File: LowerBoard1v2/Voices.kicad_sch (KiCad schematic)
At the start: 52 parts, among them J701 VoiceBoardConn_20P_200P, J702 VoiceBoardConn_20P_200P, J703 VoiceBoardConn_20P_200P, J704 VoiceBoardConn_20P_200P, J705 VoiceBoardConn_20P_200P, J706 VoiceBoardConn_20P_200P, J707 VoiceBoardConn_20P_200P, J708 VoiceBoardConn_20P_200P, U701 TCA9548APWR, U703 L7805, U704 L7905

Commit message: switched to resistor arrays for schematic
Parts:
- removed J702, J703, J704, J705, J706, J707, J708: VoiceBoardConn_20P_200P, Connector_PinHeader_2.00mm:PinHeader_2x10_P2.00mm_Vertical, symbol Connector_Audio:VoiceBoardConn_20P_200P
- removed R704, R705, R706, R707, R708, R709, R710, R711, R712, R713, R714, R715, R717, R718, R719, R720: 2k2, Resistor_SMD:R_0805_2012Metric, symbol Device:R_US
- added J502, J503, J504, J505, J506, J507, J508: VoiceBoardConn_20P_200P, Connector_PinHeader_2.00mm:PinHeader_2x10_P2.00mm_Vertical, symbol Connector_Audio:VoiceBoardConn_20P_200P
- added RN501, RN502, RN503, RN504: 2k2, Resistor_SMD:R_Array_Concave_4x0603, symbol Device:R_Pack04_Split
- renumbered C702 to C501, C705 to C502, C703 to C503, C704 to C504, C701 to C505, J701 to J501, R701 to R501, R702 to R502, R703 to R503, R716 to R504, TP701 to TP501, TP702 to TP502, TP703 to TP503, TP704 to TP504, TP705 to TP505, TP706 to TP506, TP715 to TP507, TP716 to TP508, TP707 to TP509, TP708 to TP510, TP709 to TP511, TP710 to TP512, TP711 to TP513, TP712 to TP514, TP713 to TP515, TP714 to TP516, U703 to U501, U704 to U502, U701 to U503
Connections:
- net +12V: now also J502.17 (+12V), J503.17 (+12V), J504.17 (+12V), J505.17 (+12V), J506.17 (+12V), J507.17 (+12V), J508.17 (+12V)
- net +3.3V: now also J502.15 (+3V3), J503.15 (+3V3), J504.15 (+3V3), J505.15 (+3V3), J506.15 (+3V3), J507.15 (+3V3), J508.15 (+3V3), RN501.5 (R4.2), RN501.6 (R3.2), RN501.7 (R2.2), RN501.8 (R1.2), RN502.5 (R4.2), RN502.6 (R3.2), RN502.7 (R2.2), RN502.8 (R1.2), RN503.5 (R4.2), RN503.6 (R3.2), RN503.7 (R2.2), RN503.8 (R1.2), RN504.5 (R4.2), RN504.6 (R3.2), RN504.7 (R2.2), RN504.8 (R1.2)
- net +5V: now also J502.19 (+5V), J503.19 (+5V), J504.19 (+5V), J505.19 (+5V), J506.19 (+5V), J507.19 (+5V), J508.19 (+5V)
- net -12V: now also J502.18 (-12V), J503.18 (-12V), J504.18 (-12V), J505.18 (-12V), J506.18 (-12V), J507.18 (-12V), J508.18 (-12V)
- net -5V: now also J502.20 (-5V), J503.20 (-5V), J504.20 (-5V), J505.20 (-5V), J506.20 (-5V), J507.20 (-5V), J508.20 (-5V)
- net CUTOFF_V2: now also J502.12 (VCF)
- net CUTOFF_V3: now also J503.12 (VCF)
- net CUTOFF_V4: now also J504.12 (VCF)
- net CUTOFF_V5: now also J505.12 (VCF)
- net CUTOFF_V6: now also J506.12 (VCF)
- net CUTOFF_V7: now also J507.12 (VCF)
- net CUTOFF_V8: now also J508.12 (VCF)
- net FOLD_FIRST: now also J502.11 (FF), J503.11 (FF), J504.11 (FF), J505.11 (FF), J506.11 (FF), J507.11 (FF), J508.11 (FF)
- net FOLD_V2: now also J502.10 (FOLD)
- net FOLD_V3: now also J503.10 (FOLD)
- net FOLD_V4: now also J504.10 (FOLD)
- net FOLD_V5: now also J505.10 (FOLD)
- net FOLD_V6: now also J506.10 (FOLD)
- net FOLD_V7: now also J507.10 (FOLD)
- net FOLD_V8: now also J508.10 (FOLD)
- net GND: now also J502.16 (GND), J503.16 (GND), J504.16 (GND), J505.16 (GND), J506.16 (GND), J507.16 (GND), J508.16 (GND)
- net HP_MODE: now also J502.9 (HP), J503.9 (HP), J504.9 (HP), J505.9 (HP), J506.9 (HP), J507.9 (HP), J508.9 (HP)
- net LVL1_V2: now also J502.2 (LVL1)
- net LVL1_V3: now also J503.2 (LVL1)
- net LVL1_V4: now also J504.2 (LVL1)
- net LVL1_V5: now also J505.2 (LVL1)
- net LVL1_V6: now also J506.2 (LVL1)
- net LVL1_V7: now also J507.2 (LVL1)
- net LVL1_V8: now also J508.2 (LVL1)
- net LVL2_V2: now also J502.4 (LVL2)
- net LVL2_V3: now also J503.4 (LVL2)
- net LVL2_V4: now also J504.4 (LVL2)
- net LVL2_V5: now also J505.4 (LVL2)
- net LVL2_V6: now also J506.4 (LVL2)
- net LVL2_V7: now also J507.4 (LVL2)
- net LVL2_V8: now also J508.4 (LVL2)
- net PWM1_V2: now also J502.6 (PWM1)
- net PWM1_V3: now also J503.6 (PWM1)
- net PWM1_V4: now also J504.6 (PWM1)
- net PWM1_V5: now also J505.6 (PWM1)
- net PWM1_V6: now also J506.6 (PWM1)
- net PWM1_V7: now also J507.6 (PWM1)
- net PWM1_V8: now also J508.6 (PWM1)
- net PWM2_V2: now also J502.8 (PWM2)
- net PWM2_V3: now also J503.8 (PWM2)
- net PWM2_V4: now also J504.8 (PWM2)
- net PWM2_V5: now also J505.8 (PWM2)
- net PWM2_V6: now also J506.8 (PWM2)
- net PWM2_V7: now also J507.8 (PWM2)
- net PWM2_V8: now also J508.8 (PWM2)
- net SCL_V1: now also RN501.1 (R1.1)
- net SCL_V2: now also J502.3 (SCL), RN501.3 (R3.1)
- net SCL_V3: now also J503.3 (SCL), RN502.1 (R1.1)
- net SCL_V4: now also J504.3 (SCL), RN502.3 (R3.1)
- net SCL_V5: now also J505.3 (SCL), RN503.1 (R1.1)
- net SCL_V6: now also J506.3 (SCL), RN503.3 (R3.1)
- net SCL_V7: now also J507.3 (SCL), RN504.1 (R1.1)
- net SCL_V8: now also J508.3 (SCL), RN504.3 (R3.1)
- net SDA_V1: now also RN501.2 (R2.1)
- net SDA_V2: now also J502.1 (SDA), RN501.4 (R4.1)
- net SDA_V3: now also J503.1 (SDA), RN502.2 (R2.1)
- net SDA_V4: now also J504.1 (SDA), RN502.4 (R4.1)
- net SDA_V5: now also J505.1 (SDA), RN503.2 (R2.1)
- net SDA_V6: now also J506.1 (SDA), RN503.4 (R4.1)
- net SDA_V7: now also J507.1 (SDA), RN504.2 (R2.1)
- net SDA_V8: now also J508.1 (SDA), RN504.4 (R4.1)
- net V2_CLK1: now also J502.7 (CLK2)
- net V2_CLK2: now also J502.5 (CLK1)
- net V2_OUT: now also J502.13 (OUT)
- net V3_CLK1: now also J503.7 (CLK2)
- net V3_CLK2: now also J503.5 (CLK1)
- net V3_OUT: now also J503.13 (OUT)
- net V4_CLK1: now also J504.7 (CLK2)
- net V4_CLK2: now also J504.5 (CLK1)
- net V4_OUT: now also J504.13 (OUT)
- net V5_CLK1: now also J505.7 (CLK2)
- net V5_CLK2: now also J505.5 (CLK1)
- net V5_OUT: now also J505.13 (OUT)
- net V6_CLK1: now also J506.7 (CLK2)
- net V6_CLK2: now also J506.5 (CLK1)
- net V6_OUT: now also J506.13 (OUT)
- net V7_CLK1: now also J507.7 (CLK2)
- net V7_CLK2: now also J507.5 (CLK1)
- net V7_OUT: now also J507.13 (OUT)
- net V8_CLK1: now also J508.7 (CLK2)
- net V8_CLK2: now also J508.5 (CLK1)
- net V8_OUT: now also J508.13 (OUT)
- net VCA_V2: now also J502.14 (VCA)
- net VCA_V3: now also J503.14 (VCA)
- net VCA_V4: now also J504.14 (VCA)
- net VCA_V5: now also J505.14 (VCA)
- net VCA_V6: now also J506.14 (VCA)
- net VCA_V7: now also J507.14 (VCA)
- net VCA_V8: now also J508.14 (VCA)

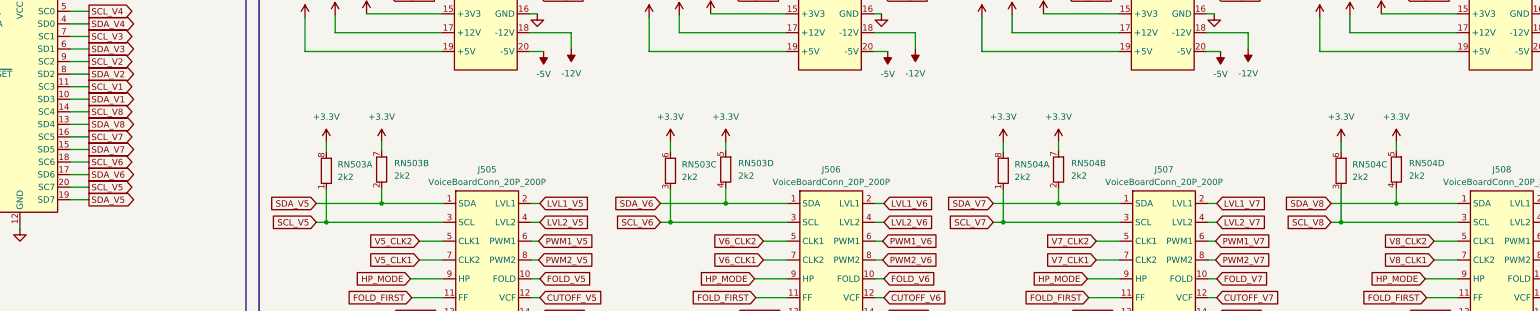
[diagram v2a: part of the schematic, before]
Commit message: clock & I2C routing
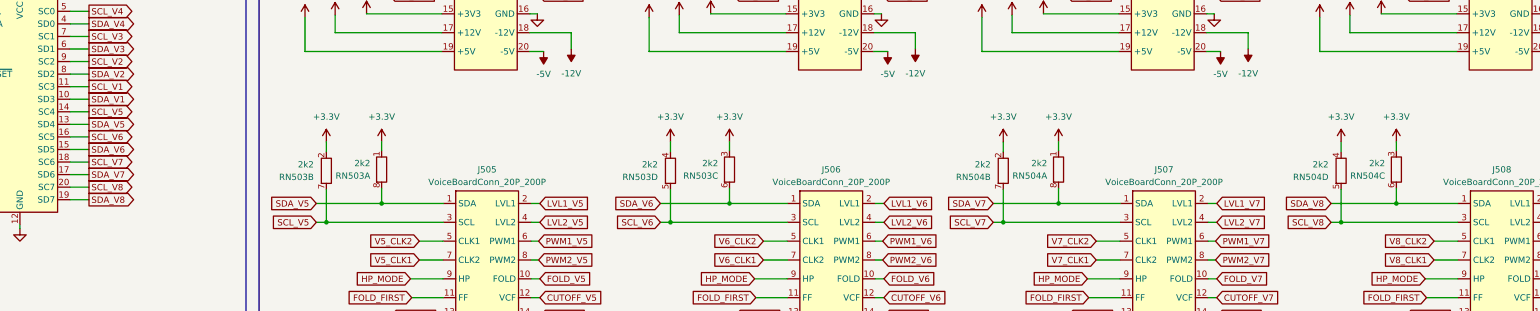
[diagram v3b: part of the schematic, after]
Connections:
- net +3.3V: now also RN503.1 (R1.1), RN503.2 (R2.1), RN503.3 (R3.1), RN503.4 (R4.1), RN504.1 (R1.1), RN504.2 (R2.1), RN504.3 (R3.1), RN504.4 (R4.1); no longer RN503.5 (R4.2), RN503.6 (R3.2), RN503.7 (R2.2), RN503.8 (R1.2), RN504.5 (R4.2), RN504.6 (R3.2), RN504.7 (R2.2), RN504.8 (R1.2)
- net SCL_V5: now also RN503.7 (R2.2), U503.14 (SC4); no longer RN503.1 (R1.1), U503.20 (SC7)
- net SCL_V6: now also RN503.5 (R4.2), U503.16 (SC5); no longer RN503.3 (R3.1), U503.18 (SC6)
- net SCL_V7: now also RN504.7 (R2.2), U503.18 (SC6); no longer RN504.1 (R1.1), U503.16 (SC5)
- net SCL_V8: now also RN504.5 (R4.2), U503.20 (SC7); no longer RN504.3 (R3.1), U503.14 (SC4)
- net SDA_V5: now also RN503.8 (R1.2), U503.13 (SD4); no longer RN503.2 (R2.1), U503.19 (SD7)
- net SDA_V6: now also RN503.6 (R3.2), U503.15 (SD5); no longer RN503.4 (R4.1), U503.17 (SD6)
- net SDA_V7: now also RN504.8 (R1.2), U503.17 (SD6); no longer RN504.2 (R2.1), U503.15 (SD5)
- net SDA_V8: now also RN504.6 (R3.2), U503.19 (SD7); no longer RN504.4 (R4.1), U503.13 (SD4)
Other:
- moved on the sheet: RN503A, RN503B, RN503C, RN503D, RN504A, RN504B, RN504C, RN504D

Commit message: power supply and load switch stuff
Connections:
- net SCL_V1: now also RN501.3 (R3.1), U503.5 (SC0); no longer RN501.1 (R1.1), U503.11 (SC3)
- net SCL_V2: now also RN501.1 (R1.1), U503.7 (SC1); no longer RN501.3 (R3.1), U503.9 (SC2)
- net SCL_V3: now also RN502.3 (R3.1), U503.9 (SC2); no longer RN502.1 (R1.1), U503.7 (SC1)
- net SCL_V4: now also RN502.1 (R1.1), U503.11 (SC3); no longer RN502.3 (R3.1), U503.5 (SC0)
- net SDA_V1: now also RN501.4 (R4.1), U503.4 (SD0); no longer RN501.2 (R2.1), U503.10 (SD3)
- net SDA_V2: now also RN501.2 (R2.1), U503.6 (SD1); no longer RN501.4 (R4.1), U503.8 (SD2)
- net SDA_V3: now also RN502.4 (R4.1), U503.8 (SD2); no longer RN502.2 (R2.1), U503.6 (SD1)
- net SDA_V4: now also RN502.2 (R2.1), U503.10 (SD3); no longer RN502.4 (R4.1), U503.4 (SD0)
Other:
- moved on the sheet: RN501A, RN501B, RN501C, RN501D, RN502A, RN502B, RN502C, RN502D
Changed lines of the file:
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@@
 	(global_label "SCL_V2"
 		(shape output)
-		(at 87.122 83.312 0)
+		(at 87.122 78.232 0)
 		(fields_autoplaced yes)
 		(effects
@@
 		)
 		(property "Intersheetrefs" "${INTERSHEET_REFS}"
-			(at 96.8805 83.312 0)
+			(at 96.8805 78.232 0)
 			(effects
 				(font
@@
 	(global_label "SCL_V3"
 		(shape output)
-		(at 87.122 78.232 0)
+		(at 87.122 83.312 0)
 		(fields_autoplaced yes)
 		(effects
@@
 		)
 		(property "Intersheetrefs" "${INTERSHEET_REFS}"
-			(at 96.8805 78.232 0)
+			(at 96.8805 83.312 0)
 			(effects
 				(font
@@
 	(global_label "SCL_V1"
 		(shape output)
-		(at 87.122 88.392 0)
+		(at 87.122 73.152 0)
 		(fields_autoplaced yes)
 		(effects
@@
 		)
 		(property "Intersheetrefs" "${INTERSHEET_REFS}"
-			(at 96.8805 88.392 0)
+			(at 96.8805 73.152 0)
 			(effects
 				(font
@@
 	(global_label "SCL_V4"
 		(shape output)
-		(at 87.122 73.152 0)
+		(at 87.122 88.392 0)
 		(fields_autoplaced yes)
 		(effects
@@
 		)
 		(property "Intersheetrefs" "${INTERSHEET_REFS}"
-			(at 96.8805 73.152 0)
+			(at 96.8805 88.392 0)
 			(effects
 				(font
@@
 	(global_label "SDA_V4"
 		(shape output)
-		(at 87.122 75.692 0)
+		(at 87.122 90.932 0)
 		(fields_autoplaced yes)
 		(effects
@@
 		)
 		(property "Intersheetrefs" "${INTERSHEET_REFS}"
-			(at 96.941 75.692 0)
+			(at 96.941 90.932 0)
 			(effects
 				(font
@@
 	(global_label "SDA_V1"
 		(shape output)
-		(at 87.122 90.932 0)
+		(at 87.122 75.692 0)
 		(fields_autoplaced yes)
 		(effects
@@
 		)
 		(property "Intersheetrefs" "${INTERSHEET_REFS}"
-			(at 96.941 90.932 0)
+			(at 96.941 75.692 0)
 			(effects
 				(font
@@
 	(global_label "SDA_V3"
 		(shape output)
-		(at 87.122 80.772 0)
+		(at 87.122 85.852 0)
 		(fields_autoplaced yes)
 		(effects
@@
 		)
 		(property "Intersheetrefs" "${INTERSHEET_REFS}"
-			(at 96.941 80.772 0)
+			(at 96.941 85.852 0)
 			(effects
 				(font
@@
 	(global_label "SDA_V2"
 		(shape output)
-		(at 87.122 85.852 0)
+		(at 87.122 80.772 0)
 		(fields_autoplaced yes)
 		(effects
@@
 		)
 		(property "Intersheetrefs" "${INTERSHEET_REFS}"
-			(at 96.941 85.852 0)
+			(at 96.941 80.772 0)
 			(effects
 				(font
@@
 	(symbol
 		(lib_id "Device:R_Pack04_Split")
-		(at 146.05 40.132 0)
+		(at 215.646 40.132 0)
 		(unit 2)
 		(exclude_from_sim no)
@@
 		(fields_autoplaced yes)
 		(property "Reference" "RN501"
-			(at 148.59 38.8619 0)
+			(at 218.186 38.8619 0)
 			(effects
 				(font
@@
 		)
 		(property "Value" "2k2"
-			(at 148.59 41.4019 0)
+			(at 218.186 41.4019 0)
 			(effects
 				(font
@@
 		)
 		(property "Footprint" "Resistor_SMD:R_Array_Concave_4x0603"
-			(at 144.018 40.132 90)
+			(at 213.614 40.132 90)
 			(effects
 				(font
@@
 		)
 		(property "Datasheet" "~"
-			(at 146.05 40.132 0)
+			(at 215.646 40.132 0)
 			(effects
 				(font
@@
 		)
 		(property "Description" "4 resistor network, parallel topology, split"
-			(at 146.05 40.132 0)
+			(at 215.646 40.132 0)
 			(effects
 				(font
@@
 	(symbol
 		(lib_id "Device:R_Pack04_Split")
-		(at 340.106 40.386 0)
+		(at 271.78 40.386 0)
 		(unit 3)
 		(exclude_from_sim no)
@@
 		(fields_autoplaced yes)
 		(property "Reference" "RN502"
-			(at 342.392 39.1159 0)
+			(at 274.066 39.1159 0)
 			(effects
 				(font
@@
 		)
 		(property "Value" "2k2"
-			(at 342.392 41.6559 0)
+			(at 274.066 41.6559 0)
 			(effects
 				(font
@@
 		)
 		(property "Footprint" "Resistor_SMD:R_Array_Concave_4x0603"
-			(at 338.074 40.386 90)
+			(at 269.748 40.386 90)
 			(effects
 				(font
@@
 		)
 		(property "Datasheet" "~"
-			(at 340.106 40.386 0)
+			(at 271.78 40.386 0)
 			(effects
 				(font
@@
 		)
 		(property "Description" "4 resistor network, parallel topology, split"
-			(at 340.106 40.386 0)
+			(at 271.78 40.386 0)
 			(effects
 				(font
@@
 	(symbol
 		(lib_id "Device:R_Pack04_Split")
-		(at 134.874 40.386 0)
+		(at 204.47 40.386 0)
 		(unit 1)
 		(exclude_from_sim no)
@@
 		(fields_autoplaced yes)
 		(property "Reference" "RN501"
-			(at 137.16 39.1159 0)
+			(at 206.756 39.1159 0)
 			(effects
 				(font
@@
 		)
 		(property "Value" "2k2"
-			(at 137.16 41.6559 0)
+			(at 206.756 41.6559 0)
 			(effects
 				(font
@@
 		)
 		(property "Footprint" "Resistor_SMD:R_Array_Concave_4x0603"
-			(at 132.842 40.386 90)
+			(at 202.438 40.386 90)
 			(effects
 				(font
@@
 		)
 		(property "Datasheet" "~"
-			(at 134.874 40.386 0)
+			(at 204.47 40.386 0)
 			(effects
 				(font
@@
 		)
 		(property "Description" "4 resistor network, parallel topology, split"
-			(at 134.874 40.386 0)
+			(at 204.47 40.386 0)
 			(effects
 				(font
@@
 	(symbol
 		(lib_id "Device:R_Pack04_Split")
-		(at 215.646 40.132 0)
+		(at 146.05 40.132 0)
 		(unit 4)
 		(exclude_from_sim no)
@@
 		(fields_autoplaced yes)
 		(property "Reference" "RN501"
-			(at 218.186 38.8619 0)
+			(at 148.59 38.8619 0)
 			(effects
 				(font
@@
 		)
 		(property "Value" "2k2"
-			(at 218.186 41.4019 0)
+			(at 148.59 41.4019 0)
 			(effects
 				(font
@@
 		)
 		(property "Footprint" "Resistor_SMD:R_Array_Concave_4x0603"
-			(at 213.614 40.132 90)
+			(at 144.018 40.132 90)
 			(effects
 				(font
@@
 		)
 		(property "Datasheet" "~"
-			(at 215.646 40.132 0)
+			(at 146.05 40.132 0)
 			(effects
 				(font
@@
 		)
 		(property "Description" "4 resistor network, parallel topology, split"
-			(at 215.646 40.132 0)
+			(at 146.05 40.132 0)
 			(effects
 				(font
@@
 	(symbol
 		(lib_id "Device:R_Pack04_Split")
-		(at 271.78 40.386 0)
+		(at 340.106 40.386 0)
 		(unit 1)
 		(exclude_from_sim no)
@@
 		(fields_autoplaced yes)
 		(property "Reference" "RN502"
-			(at 274.066 39.1159 0)
+			(at 342.392 39.1159 0)
 			(effects
 				(font
@@
 		)
 		(property "Value" "2k2"
-			(at 274.066 41.6559 0)
+			(at 342.392 41.6559 0)
 			(effects
 				(font
@@
 		)
 		(property "Footprint" "Resistor_SMD:R_Array_Concave_4x0603"
-			(at 269.748 40.386 90)
+			(at 338.074 40.386 90)
 			(effects
 				(font
@@
 		)
 		(property "Datasheet" "~"
-			(at 271.78 40.386 0)
+			(at 340.106 40.386 0)
 			(effects
 				(font
@@
 		)
 		(property "Description" "4 resistor network, parallel topology, split"
-			(at 271.78 40.386 0)
+			(at 340.106 40.386 0)
 			(effects
 				(font
@@
 	(symbol
 		(lib_id "Device:R_Pack04_Split")
-		(at 282.956 40.132 0)
+		(at 351.282 40.132 0)
 		(unit 2)
 		(exclude_from_sim no)
@@
 		(fields_autoplaced yes)
 		(property "Reference" "RN502"
-			(at 285.496 38.8619 0)
+			(at 353.822 38.8619 0)
 			(effects
 				(font
@@
 		)
 		(property "Value" "2k2"
-			(at 285.496 41.4019 0)
+			(at 353.822 41.4019 0)
 			(effects
 				(font
@@
 		)
 		(property "Footprint" "Resistor_SMD:R_Array_Concave_4x0603"
-			(at 280.924 40.132 90)
+			(at 349.25 40.132 90)
 			(effects
 				(font
@@
 		)
 		(property "Datasheet" "~"
-			(at 282.956 40.132 0)
+			(at 351.282 40.132 0)
 			(effects
 				(font
@@
 		)
 		(property "Description" "4 resistor network, parallel topology, split"
-			(at 282.956 40.132 0)
+			(at 351.282 40.132 0)
 			(effects
 				(font
@@
 	(symbol
 		(lib_id "Device:R_Pack04_Split")
-		(at 204.47 40.386 0)
+		(at 134.874 40.386 0)
 		(unit 3)
 		(exclude_from_sim no)
@@
 		(fields_autoplaced yes)
 		(property "Reference" "RN501"
-			(at 206.756 39.1159 0)
+			(at 137.16 39.1159 0)
 			(effects
 				(font
@@
 		)
 		(property "Value" "2k2"
-			(at 206.756 41.6559 0)
+			(at 137.16 41.6559 0)
 			(effects
 				(font
@@
 		)
 		(property "Footprint" "Resistor_SMD:R_Array_Concave_4x0603"
-			(at 202.438 40.386 90)
+			(at 132.842 40.386 90)
 			(effects
 				(font
@@
 		)
 		(property "Datasheet" "~"
-			(at 204.47 40.386 0)
+			(at 134.874 40.386 0)
 			(effects
 				(font
@@
 		)
 		(property "Description" "4 resistor network, parallel topology, split"
-			(at 204.47 40.386 0)
+			(at 134.874 40.386 0)
 			(effects
 				(font
@@
 	(symbol
 		(lib_id "Device:R_Pack04_Split")
-		(at 351.282 40.132 0)
+		(at 282.956 40.132 0)
 		(unit 4)
 		(exclude_from_sim no)
@@
 		(fields_autoplaced yes)
 		(property "Reference" "RN502"
-			(at 353.822 38.8619 0)
+			(at 285.496 38.8619 0)
 			(effects
 				(font
@@
 		)
 		(property "Value" "2k2"
-			(at 353.822 41.4019 0)
+			(at 285.496 41.4019 0)
 			(effects
 				(font
@@
 		)
 		(property "Footprint" "Resistor_SMD:R_Array_Concave_4x0603"
-			(at 349.25 40.132 90)
+			(at 280.924 40.132 90)
 			(effects
 				(font
@@
 		)
 		(property "Datasheet" "~"
-			(at 351.282 40.132 0)
+			(at 282.956 40.132 0)
 			(effects
 				(font
@@
 		)
 		(property "Description" "4 resistor network, parallel topology, split"
-			(at 351.282 40.132 0)
+			(at 282.956 40.132 0)
 			(effects
 				(font
